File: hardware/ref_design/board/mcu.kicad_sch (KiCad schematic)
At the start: 12 parts, among them U4 RP2354B, X1 12MHz

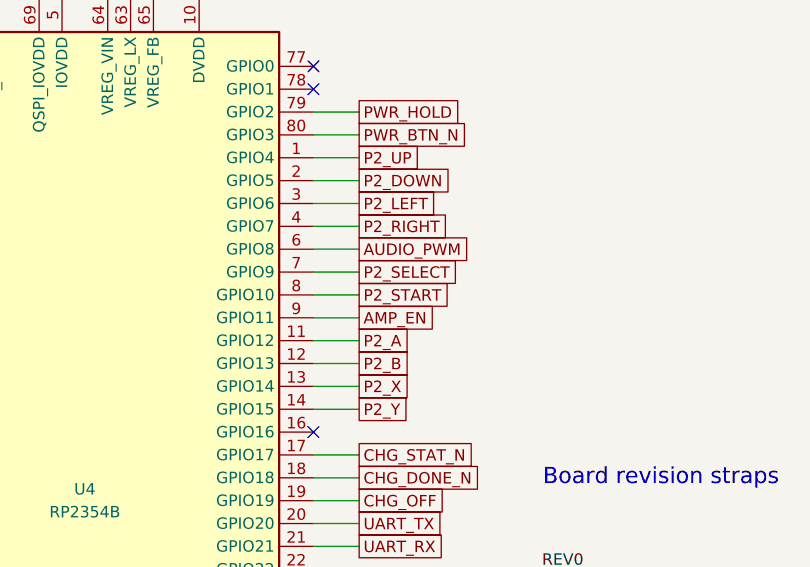
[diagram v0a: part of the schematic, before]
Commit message: WIP: row 19 layout, one-sided: no speaker, core in the left bezel (unrouted)
Since the one-sided-assembly ruling the work has been row 19, not row 18:
the speaker, J4 and the FM8002A circuit are out of design.py (GPIO8 and
GPIO11 unconnected), the cell sits in its hole, every SMT part is on the
front, and the RP2354B core moved from the back to the left bezel. Row 18
was ruled out on geometry first: with the core on the front it needs most of
one side bezel, and the speaker hole, J4 and three SOIC-8s had nowhere left.

Earlier row-19 placements (core in the right bezel) left 18-30 connections
open after Freerouting: J1's pads faced the cell hole with 1.3 mm to spare,
and seat 2's lines had to cross the whole board past the charger. This
commit has the core and the charger swapped, the hole's lead pocket cut to
1 mm and the original pin map; not routed yet.

Co-Authored-By: Claude Opus 5.5 <noreply@anthropic.com>
Claude-Session: https://claude.ai/code/session_01Y3mFMxLYqNeyyedvbYuRwX
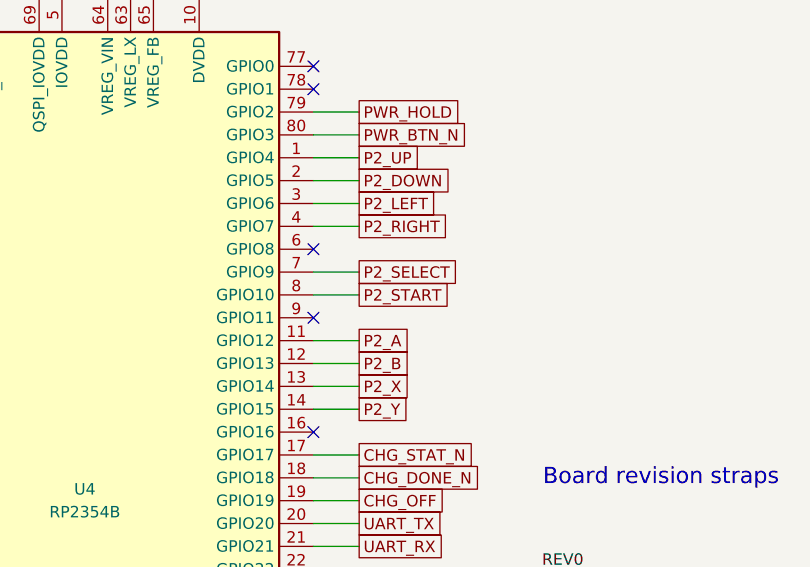
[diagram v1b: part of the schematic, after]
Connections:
- net AMP_EN: no longer names the net of U4.9 (GPIO11)
- net AUDIO_PWM: no longer names the net of U4.6 (GPIO8)
- no-connect marks 10 -> 12
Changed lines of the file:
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@@
+	)
+	(no_connect
+		(at 166.37 68.58)
+	)
+	(no_connect
+		(at 166.37 76.2)
 	)
 	(no_connect
@@
 	(wire
 		(pts
-			(xy 166.37 68.58) (xy 171.45 68.58)
-		)
-		(stroke
-			(width 0)
-			(type default)
-		)
-	)
-	(wire
-		(pts
 			(xy 166.37 71.12) (xy 171.45 71.12)
 		)
@@
 		(pts
 			(xy 166.37 73.66) (xy 171.45 73.66)
-		)
-		(stroke
-			(width 0)
-			(type default)
-		)
-	)
-	(wire
-		(pts
-			(xy 166.37 76.2) (xy 171.45 76.2)
 		)
 		(stroke
@@
 		)
 	)
-	(global_label "AUDIO_PWM"
-		(shape passive)
-		(at 171.45 68.58 0)
-		(fields_autoplaced yes)
-		(effects
-			(font
-				(size 1.27 1.27)
-			)
-			(justify left)
-		)
-		(property "Intersheetrefs" "${INTERSHEET_REFS}"
-			(at 171.45 68.58 0)
-			(hide yes)
-			(show_name no)
-			(do_not_autoplace no)
-			(effects
-				(font
-					(size 1.27 1.27)
-				)
-			)
-		)
-	)
 	(global_label "P2_SELECT"
 		(shape passive)
@@
 			(hide yes)
 			(show_name no)
-			(do_not_autoplace no)
-			(effects
-				(font
-					(size 1.27 1.27)
-				)
-			)
-		)
-	)
-	(global_label "AMP_EN"
-		(shape passive)
-		(at 171.45 76.2 0)
-		(fields_autoplaced yes)
-		(effects
-			(font
-				(size 1.27 1.27)
-			)
-			(justify left)
-		)
-		(property "Intersheetrefs" "${INTERSHEET_REFS}"
-			(at 171.45 76.2 0)
-			(hide yes)
-			(show_name no)

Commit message: WIP: row 19 with shift registers and rows 1, 4, 16; 2 nets unrouted
The cell in a 54.0 x 37.0 mm hole, no speaker, every machine-placed part on
the top. New since the last WIP: each seat's D-pad and A/B/X/Y through a
74HC165 (SN74HC165PWR, chained, SR_PL/SR_CLK/SR_DATA on GPIO28-30, 10k
arrays); seat 2's Start powers on too (D8, R62, Q7, R63; P2_START on
GPIO34); Start/Select on 4 mm metal dome footprints; the BQ24073 power-path
charger in place of the TP4056 and its load sharing (pin reviews written);
the LDO beside the core; side screws at case (+-31.4, +-36); J1 at case
y -11. GPIO8 and GPIO11 (audio) unconnected.

Checks: check_netlist, check_pins and ERC pass (0). DRC: 0 errors, 8
cosmetic silkscreen warnings, 2 unconnected: QSPI_SS (U4 pin 75 to its
3.5 mm stub) and P1_SELECT (U4 pin 44 to SW20). check_fit: 17, all from
the case not knowing the moved screws, J1 and the dome vents yet.

Co-Authored-By: Claude Opus 5.5 <noreply@anthropic.com>
Claude-Session: https://claude.ai/code/session_01Y3mFMxLYqNeyyedvbYuRwX
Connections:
- net P1_A is gone; now on net CHG_OFF: U4.54 (GPIO43/ADC3)
- net P1_B is gone; now on net CHG_STAT_N: U4.52 (GPIO41/ADC1)
- net P1_Y is gone; now on net P2_START: U4.43 (GPIO34)
- net CHG_OFF: no longer U4.19 (GPIO19)
- net CHG_STAT_N: no longer U4.17 (GPIO17)
- net P2_START: no longer U4.8 (GPIO10)
- net CHG_DONE_N: no longer names the net of U4.18 (GPIO18)
- net P1_DOWN renamed SR_CLK
- net P1_LEFT renamed SR_DATA
- net P1_RIGHT: no longer names the net of U4.39 (GPIO31)
- net P1_UP renamed SR_PL
- net P1_X renamed CHG_PG_N
- net P2_A: no longer names the net of U4.11 (GPIO12)
- net P2_B: no longer names the net of U4.12 (GPIO13)
- net P2_DOWN: no longer names the net of U4.2 (GPIO5)
- net P2_LEFT: no longer names the net of U4.3 (GPIO6)
- net P2_RIGHT: no longer names the net of U4.4 (GPIO7)
- net P2_UP: no longer names the net of U4.1 (GPIO4)
- net P2_X: no longer names the net of U4.13 (GPIO14)
- net P2_Y: no longer names the net of U4.14 (GPIO15)
- no-connect marks 12 -> 25

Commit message: ref_design: strips review: USB pair, SR_CLK series resistor, strip stitching, pinmap
Review of the strips beside the cell's hole (rows 1-4 of the review):
- USB D+/D-: route.py's usb_pair() draws them as one pair (0.2 mm, 0.3 apart) from
  J1 (D+ pads joined behind A7, D- at their tips) through U1, turned so each line
  runs over its own pin with no stub, then on the back to R21/R22. C1/R41 moved
  below the pair.
- SR_CLK: R65 (33 ohm, C25105, Basic) in series at the RP2354B's end, about 12 mm
  of track from pin 37, clear of the folded FPC. A 0.4 mm clock-to-SR_PL/SR_DATA
  clearance rule (and a GND guard track along each strip) left SR_CLK or SR_PL to
  U9 unrouted in five runs, so neither is in this board.
- Ground: strip_stitch() adds GND vias in the strips wherever both pours are filled.
- Flex: C47 turned with its long axis along the strip; the case asked for floor
  ribs under the strips (CELLCUT_FOR_CASE.md).
- docs/pinmap.md: both Starts as power buttons, SR_PL/SR_CLK/SR_DATA roles, the
  BQ24073 charger (no TP4056, CHG_DONE_N, D5/D7/Q2), 27 ohm USB resistors.

Routed clean (seed 7): DRC 0 errors, 0 unconnected; check_netlist, check_pins,
ERC pass; check_fit 17, the known case-side items.

Co-Authored-By: Claude Opus 5.5 <noreply@anthropic.com>
Claude-Session: https://claude.ai/code/session_01Y3mFMxLYqNeyyedvbYuRwX
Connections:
- net SR_CLK renamed SR_CLK_MCU
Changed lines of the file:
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@@
 		)
 	)
-	(global_label "SR_CLK"
+	(global_label "SR_CLK_MCU"
 		(shape passive)
 		(at 171.45 121.92 0)

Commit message: WIP: speaker on the board's top in the right bezel, audio back; 5 nets unrouted
The FM8002A circuit returns as before row 19 (GPIO8 AUDIO_PWM, GPIO11 AMP_EN,
gain 2, J4 PicoBlade for the speaker's plug). The speaker (15 x 10, hand-fitted)
lies face up in the right bezel below the cell's hole: a rule area keeps parts
(not copper) out of it plus 0.5 mm, outline and label on the silkscreen. J1,
the speaker and J4 with its plug don't all fit in that bezel, so J1 went back up
its wall to the case's own y (beside the hole); usb_pair() drops the pair to the
back beside J1's pads. J4 is machine-placed again (out of NO_ASSEMBLY).

Open: 5 connections (CHG_TEMP, CHG_OFF, CC2_SENSE, SR_CLK, a GND pour island),
route.py --finish crashes in Space() (SwigPyObject), Q3 in the cluster's 0.5 mm
retainer band. case/CELLCUT_FOR_CASE.md has the speaker, grille and J4 notes.

Co-Authored-By: Claude Opus 5.5 <noreply@anthropic.com>
Claude-Session: https://claude.ai/code/session_01Y3mFMxLYqNeyyedvbYuRwX
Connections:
- net AUDIO_PWM: now reaches U4.6 (GPIO8)
- net AMP_EN: now reaches U4.9 (GPIO11)
- no-connect marks 25 -> 23
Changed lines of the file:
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@@
-	)
-	(no_connect
-		(at 166.37 68.58)
 	)
 	(no_connect
@@
 	)
 	(no_connect
-		(at 166.37 76.2)
-	)
-	(no_connect
 		(at 166.37 78.74)
 	)
@@
 	(wire
 		(pts
+			(xy 166.37 68.58) (xy 171.45 68.58)
+		)
+		(stroke
+			(width 0)
+			(type default)
+		)
+	)
+	(wire
+		(pts
 			(xy 166.37 71.12) (xy 171.45 71.12)
+		)
+		(stroke
+			(width 0)
+			(type default)
+		)
+	)
+	(wire
+		(pts
+			(xy 166.37 76.2) (xy 171.45 76.2)
 		)
 		(stroke
@@
 		)
 	)
+	(global_label "AUDIO_PWM"
+		(shape passive)
+		(at 171.45 68.58 0)
+		(fields_autoplaced yes)
+		(effects
+			(font
+				(size 1.27 1.27)
+			)
+			(justify left)
+		)
+		(property "Intersheetrefs" "${INTERSHEET_REFS}"
+			(at 171.45 68.58 0)
+			(hide yes)
+			(show_name no)
+			(do_not_autoplace no)
+			(effects
+				(font
+					(size 1.27 1.27)
+				)
+			)
+		)
+	)
 	(global_label "P2_SELECT"
 		(shape passive)
@@
 			(hide yes)
 			(show_name no)
+			(do_not_autoplace no)
+			(effects
+				(font
+					(size 1.27 1.27)
+				)
+			)
+		)
+	)
+	(global_label "AMP_EN"
+		(shape passive)
+		(at 171.45 76.2 0)
+		(fields_autoplaced yes)
+		(effects
+			(font
+				(size 1.27 1.27)
+			)
+			(justify left)
+		)
+		(property "Intersheetrefs" "${INTERSHEET_REFS}"
+			(at 171.45 76.2 0)
+			(hide yes)
+			(show_name no)

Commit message: ref_design levers: pins facing their nets, no REV straps, no UART, debug buttons and latch parts out of the strips
An experiment for Alex (not on ref-design-cellcut): make the board easier to route without
changing its size.
1. GPIOs: AUDIO_PWM 8 -> 31 (PWM7 B), AMP_EN 11 -> 34, BL_PWM 44 -> 28 (PWM6 A), PWR_HOLD
   2 -> 44, P2_START 34 -> 2, P2_SELECT 9 -> 4, SR_PL 28 -> 19 (datasheet Table 3 checked;
   U4's pin review updated)
2. REV0-REV3 and R48-R51 removed (the revision stays on the silkscreen)
3. J6 (UART) and C41 removed; SW18/SW19 out of the left strip into the left bezel below H4
   (U3 and its caps 2 mm down, JP1 below the core)
4. The latch's strip parts (Q1, R16, R15, C47, TP6, D8, Q7, R62, R63) up past the hole's
   top edge under seat 2's deck; C42 to the right bezel
tools/strip_load.py counts nets through each strip: 11/15 -> 8/11, parts 8/16 -> 3/5.
Routed clean on the first finished attempt (seed 3, 4.2 min); check_pcb and check_fit pass.

Co-Authored-By: Claude Opus 5.5 <noreply@anthropic.com>
Claude-Session: https://claude.ai/code/session_01Y3mFMxLYqNeyyedvbYuRwX
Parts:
- removed R48: DNP, Resistor_SMD:R_0402_1005Metric, symbol Device:R
- removed R49, R50, R51: 1k, Resistor_SMD:R_0402_1005Metric, symbol Device:R
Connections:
- net AMP_EN: now also U4.43 (GPIO34); no longer U4.9 (GPIO11)
- net AUDIO_PWM: now also U4.39 (GPIO31); no longer U4.6 (GPIO8)
- net BL_PWM: now also U4.36 (GPIO28); no longer U4.55 (GPIO44/ADC4)
- net P2_SELECT: now also U4.1 (GPIO4); no longer U4.7 (GPIO9)
- net P2_START: now also U4.79 (GPIO2); no longer U4.43 (GPIO34)
- net PWR_HOLD: now also U4.55 (GPIO44/ADC4); no longer U4.79 (GPIO2)
- net SR_PL: now also U4.19 (GPIO19); no longer U4.36 (GPIO28)
- net REV0: no longer names the net of U4.22 (GPIO22)
- net REV1: no longer names the net of U4.23 (GPIO23)
- net REV2: no longer names the net of U4.25 (GPIO24)
- net REV3: no longer names the net of U4.26 (GPIO25)
- net UART_RX: no longer names the net of U4.21 (GPIO21)
- net UART_TX: no longer names the net of U4.20 (GPIO20)
- no-connect marks 23 -> 29
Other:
- note removed: "A 1k to GND makes a bit 0; a bit left unfitted"
- note removed: "Board revision straps"
- note removed: "REV = 1: R48 not fitted."
- note removed: "reads 1 through the pin's pull-up (GPIO22-25)."

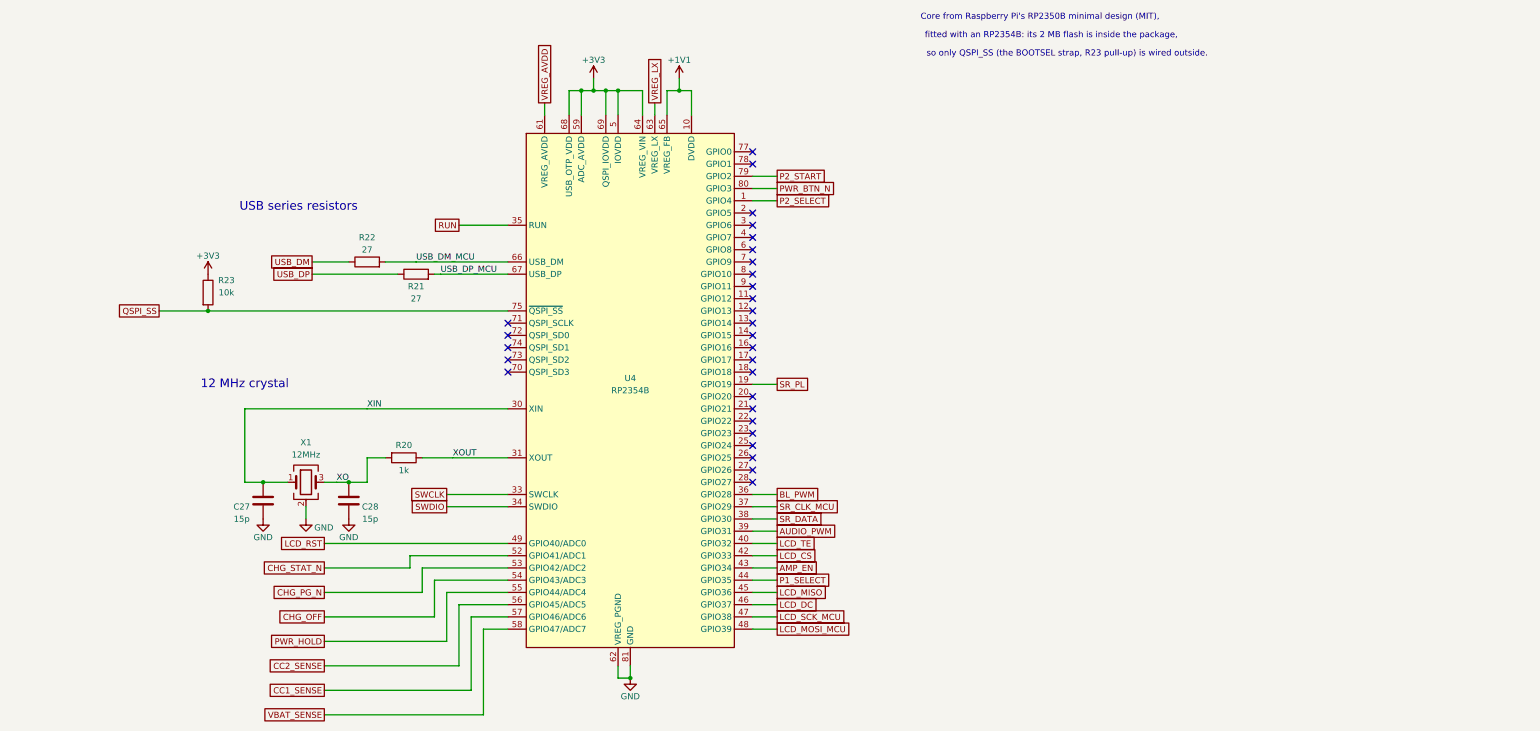
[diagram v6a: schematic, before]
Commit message: ref_design ESP32-S3 schematic: WROOM-1U-N16R8 module, TLV75733P, 8-bit 8080 panel bus (R70-R78), microSD sheet, third 74HC165, BOOT/RESET and J7 pads, 1.5k audio filter; ERC 0, netlist and pin reviews pass
Footprints: battler:ESP32-S3-WROOM-1U (KiCad's without the 0.2 mm thermal vias, tools/fp_esp32.py) and the 4-pad J7. docs/esp32s3_pinmap_diff.md lists the differences from the proposal (no GPIO differs). Unverified: JLC Basic/Extended and stock of the new parts, the DM3AT card-detect pin order.

Co-Authored-By: Claude Sonnet 5.5 <noreply@anthropic.com>
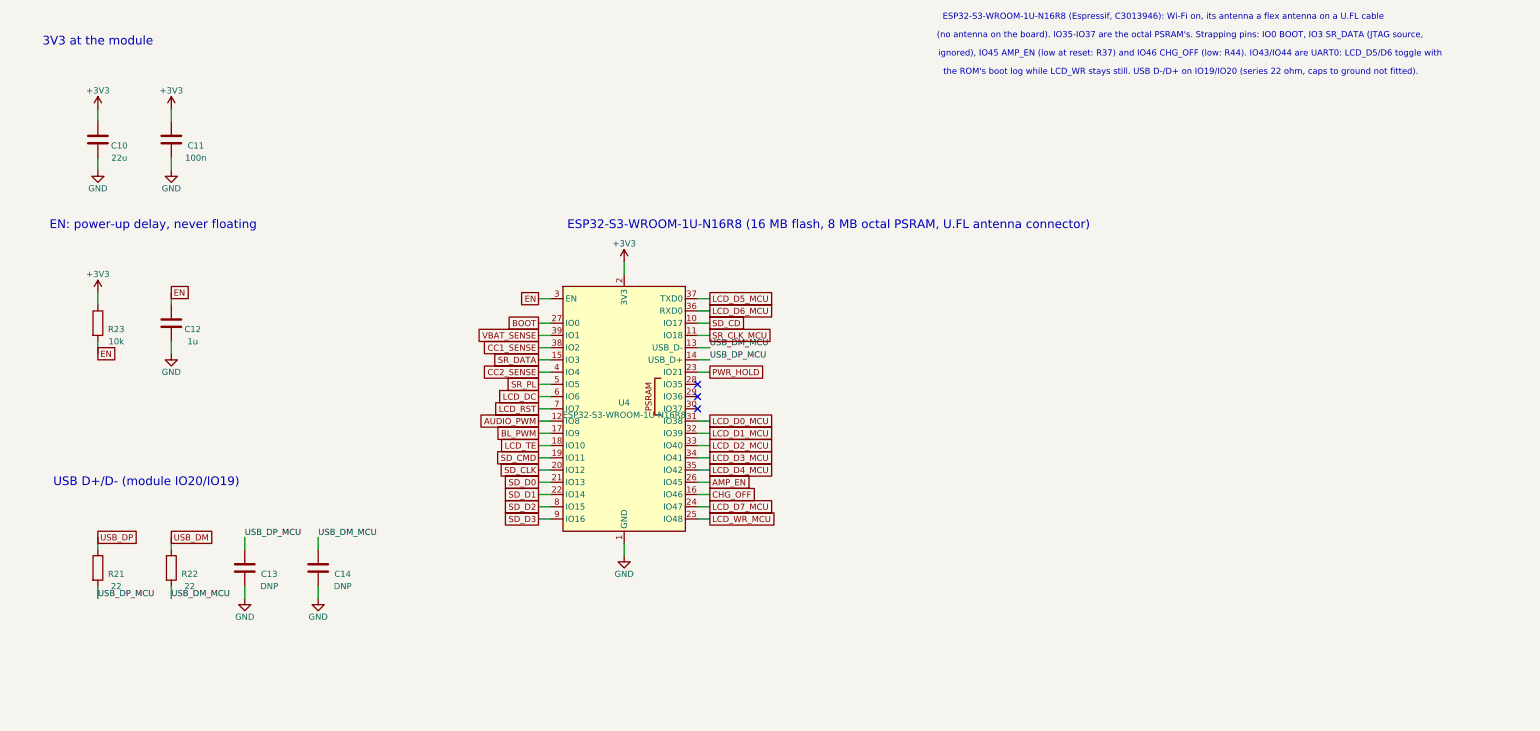
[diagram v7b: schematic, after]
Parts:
- removed C27, C28: 15p, battler:C_0402_1005Metric_RPi, symbol Device:C
- removed R20: 1k, battler:R_0402_1005Metric_RPi, symbol Device:R
- removed X1: 12MHz, battler:ABM8-272-T3, symbol Device:Crystal_GND24
- added C10: 22u, Capacitor_SMD:C_0805_2012Metric, symbol Device:C
- added C11: 100n, Capacitor_SMD:C_0402_1005Metric, symbol Device:C
- added C12: 1u, Capacitor_SMD:C_0402_1005Metric, symbol Device:C
- added C13, C14: DNP, Capacitor_SMD:C_0402_1005Metric, symbol Device:C
- R21, R22: value 27 -> 22; footprint battler:R_0402_1005Metric_RPi -> Resistor_SMD:R_0402_1005Metric; LCSC C25100 -> C25092; MPN 0402WGF270JTCE -> 0402WGF220JTCE
- R23: footprint battler:R_0402_1005Metric_RPi -> Resistor_SMD:R_0402_1005Metric
- U4: value RP2354B -> ESP32-S3-WROOM-1U-N16R8; footprint battler:RP2350B_QFN80_RPi -> battler:ESP32-S3-WROOM-1U; symbol MCU_RaspberryPi:RP2354B -> RF_Module:ESP32-S3-WROOM-1; LCSC C39843328 -> C3013946; MPN RP2354B -> ESP32-S3-WROOM-1U-N16R8; Manufacturer Raspberry Pi -> Espressif Systems
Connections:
- net P2_SELECT is gone; now on net GND: U4.1 (GND)
- net +3V3: now also U4.2 (3V3), C10.1, C11.1; no longer U4.15 (IOVDD), U4.24 (IOVDD), U4.29 (IOVDD), U4.41 (IOVDD), U4.5 (IOVDD), U4.50 (IOVDD), U4.59 (ADC_AVDD), U4.60 (IOVDD), U4.64 (VREG_VIN), U4.68 (USB_OTP_VDD), U4.69 (QSPI_IOVDD), U4.76 (IOVDD)
- net AMP_EN: now also U4.26 (IO45); no longer U4.43 (GPIO34)
- net AUDIO_PWM: now also U4.12 (IO8); no longer U4.39 (GPIO31)
- net BL_PWM: now also U4.17 (IO9); no longer U4.36 (GPIO28)
- net CC1_SENSE: now also U4.38 (IO2); no longer U4.57 (GPIO46/ADC6)
- net CC2_SENSE: now also U4.4 (IO4); no longer U4.56 (GPIO45/ADC5)
- net CHG_OFF: now also U4.16 (IO46); no longer U4.54 (GPIO43/ADC3)
- net GND: now also U4.40 (GND), U4.41 (GND), C10.2, C11.2, C12.2, C13.2, C14.2; no longer U4.62 (VREG_PGND), U4.81 (GND)
- net LCD_DC: now also U4.6 (IO6); no longer U4.46 (GPIO37)
- net LCD_RST: now also U4.7 (IO7); no longer U4.49 (GPIO40/ADC0)
- net LCD_TE: now also U4.18 (IO10); no longer U4.40 (GPIO32)
- net PWR_HOLD: now also U4.23 (IO21); no longer U4.55 (GPIO44/ADC4)
- net SR_CLK_MCU: now also U4.11 (IO18); no longer U4.37 (GPIO29)
- net SR_DATA: now also U4.15 (IO3); no longer U4.38 (GPIO30)
- net SR_PL: now also U4.5 (IO5); no longer U4.19 (GPIO19)
- net USB_DM_MCU: now also U4.13 (USB_D-), C14.1; no longer U4.66 (USB_DM)
- net USB_DP_MCU: now also U4.14 (USB_D+), C13.1; no longer U4.67 (USB_DP)
- net VBAT_SENSE: now also U4.39 (IO1); no longer U4.58 (GPIO47/ADC7)
- net SD_CLK: now reaches U4.20 (IO12)
- net SD_D0: now reaches U4.21 (IO13)
- net SD_D1: now reaches U4.22 (IO14)
- net LCD_WR_MCU: now reaches U4.25 (IO48)
- net BOOT: now reaches U4.27 (IO0)
- net EN: now reaches U4.3 (EN)
- net EN: now also R23.2, C12.1
- net SD_D2: now reaches U4.8 (IO15)
- net SD_D3: now reaches U4.9 (IO16)
- removed net +1V1: U4.10 (DVDD), U4.32 (DVDD), U4.51 (DVDD), U4.65 (VREG_FB)
- removed net CHG_PG_N: U4.53 (GPIO42/ADC2)
- removed net CHG_STAT_N: U4.52 (GPIO41/ADC1)
- removed net LCD_CS: U4.42 (GPIO33)
- removed net LCD_MISO: U4.45 (GPIO36)
- removed net LCD_MOSI_MCU: U4.48 (GPIO39)
- removed net LCD_SCK_MCU: U4.47 (GPIO38)
- removed net P1_SELECT: U4.44 (GPIO35)
- removed net P2_START: U4.79 (GPIO2)
- removed net PWR_BTN_N: U4.80 (GPIO3)
- removed net QSPI_SS: R23.2, U4.75 (~{QSPI_SS})
- net RUN renamed LCD_D4_MCU
- net SWCLK renamed LCD_D2_MCU
- net SWDIO renamed LCD_D3_MCU
- removed net VREG_AVDD: U4.61 (VREG_AVDD)
- removed net VREG_LX: U4.63 (VREG_LX)
- net XIN: no longer names the net of U4.30 (IO37)
- net XOUT renamed LCD_D0_MCU
- new net LCD_D1_MCU: U4.32 (IO39)
- new net LCD_D5_MCU: U4.37 (TXD0)
- new net LCD_D6_MCU: U4.36 (RXD0)
- new net LCD_D7_MCU: U4.24 (IO47)
- new net SD_CD: U4.10 (IO17)
- new net SD_CMD: U4.19 (IO11)
- no-connect marks 29 -> 3
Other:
- note added: "(no antenna on the board). IO35-IO37 are the octal PSRAM's. Strapping pins: IO0 BOOT, IO3 SR_DATA (JTAG source,"
- note added: "3V3 at the module"
- note added: "EN: power-up delay, never floating"
- note added: "ESP32-S3-WROOM-1U-N16R8 (16 MB flash, 8 MB octal PSRAM, U.FL antenna connector)"
- note added: "ESP32-S3-WROOM-1U-N16R8 (Espressif, C3013946): Wi-Fi on, its antenna a flex antenna on a U.FL cable"
- note added: "USB D+/D- (module IO20/IO19)"
- note added: "ignored), IO45 AMP_EN (low at reset: R37) and IO46 CHG_OFF (low: R44). IO43/IO44 are UART0: LCD_D5/D6 toggle with"
- note added: "the ROM's boot log while LCD_WR stays still. USB D-/D+ on IO19/IO20 (series 22 ohm, caps to ground not fitted)."
- note removed: "12 MHz crystal"
- note removed: "Core from Raspberry Pi's RP2350B minimal design (MIT),"
- note removed: "USB series resistors"
- note removed: "fitted with an RP2354B: its 2 MB flash is inside the package,"
- note removed: "so only QSPI_SS (the BOOTSEL strap, R23 pull-up) is wired outside."
- title: RP2354B -> ESP32-S3-WROOM-1U-N16R8
- moved on the sheet: R21, R22, R23
